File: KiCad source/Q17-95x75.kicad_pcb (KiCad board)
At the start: 2 copper layers, 96.5 x 76.2 mm, 84 parts, among them J1 TerminalBlock, Q1 IRF610, Q10 KSA992, Q11 BS250P, Q12 KSC1845, Q13 IRF610, Q14 IRF9610, Q15 FQA46N15, Q16 FQA36P15, Q2 KSA992, Q3 KSC1845, Q4 IRF9610, Q5 IRF9610, Q6 IRF610, Q7 KSC1845, Q8 2N7000, Q9 BS250P, U1 DIP-8_W7.62mm_Socket, U1 OPA1641

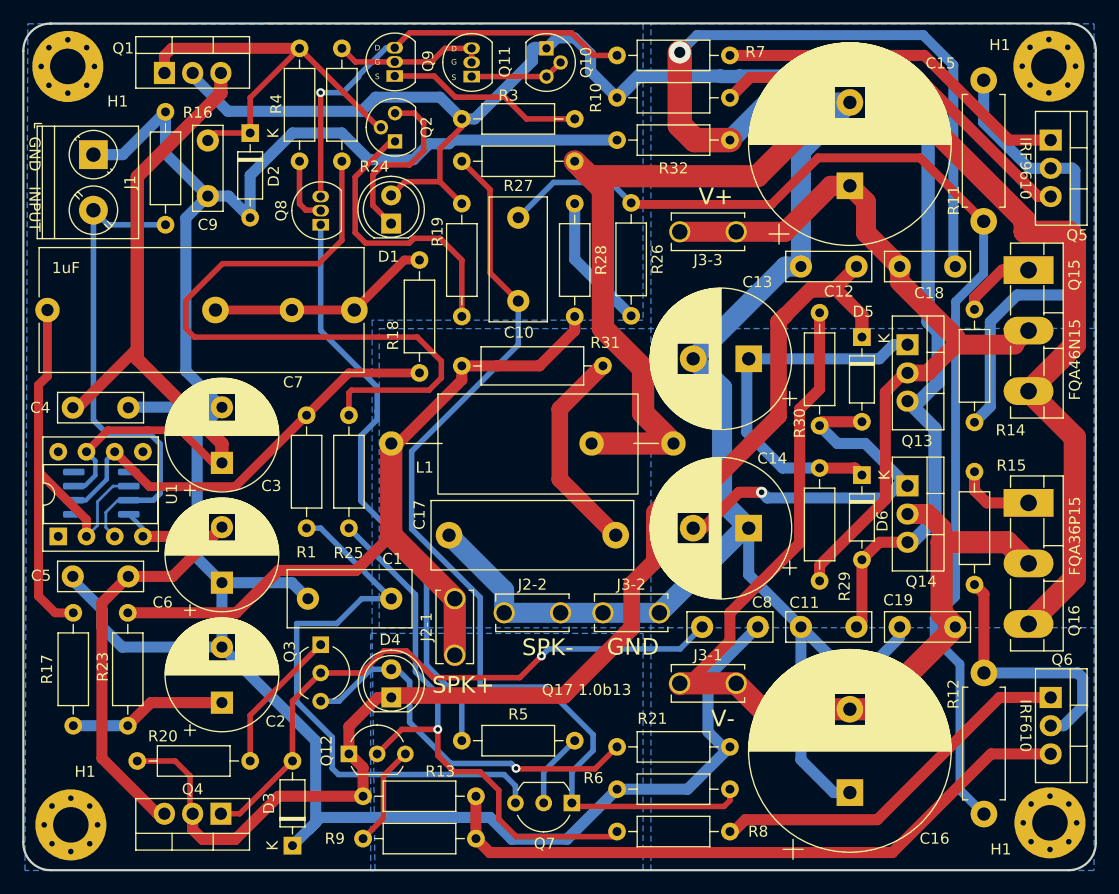
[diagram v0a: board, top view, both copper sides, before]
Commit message: Update PCB to 1.0b15
- Change Q12 footprint to TO-126.
- More cleanup of tracks.
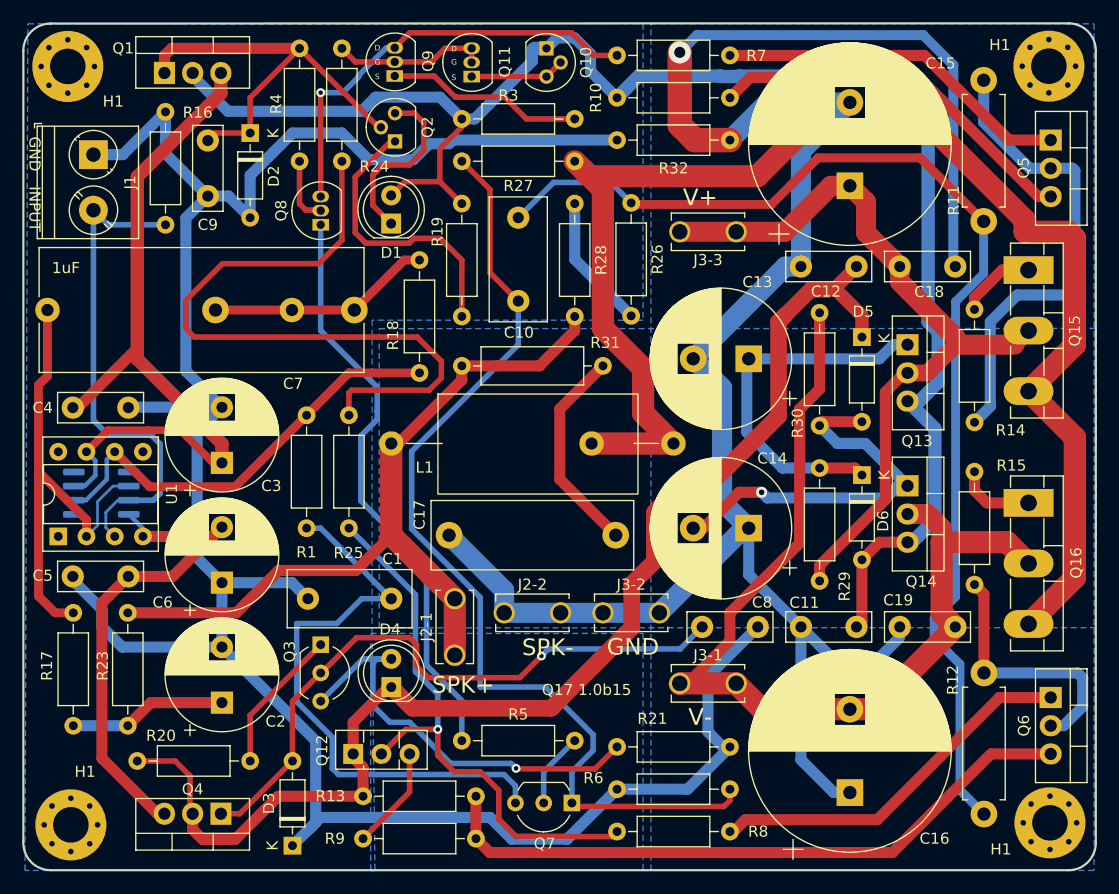
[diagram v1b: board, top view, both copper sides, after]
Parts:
- Q12: value KSC1845 -> BD139; footprint Package_TO_SOT_THT:TO-92_Inline_Wide -> Package_TO_SOT_THT:TO-126-3_Vertical
- moved D4 0.93 mm to (124.7, 111.8)
- moved Q12 0.38 mm to (121.3, 117.8)
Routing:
- net Net-(D4-Pad2): track 34.5 -> 38.7 mm
- net Net-(C8-Pad2): track 55.4 -> 57.5 mm
- net Net-(C12-Pad2): track 111.4 -> 112.3 mm
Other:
- board text added: "Q17 1.0b15"
- board text added: "QUAD405 Audiophile Tiberiu Vicol PCB Design by Stef PROTO RELEASE"
- board text removed: "FQA36P15"
- board text removed: "FQA46N15"
- board text removed: "IRF610"
- board text removed: "IRF9610"
- board text removed: "Q17 1.0b13"
- board text removed: "QUAD405 Audiophile Tiberiu Vicol PCB Design by Stef"

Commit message: PCB and diagram v1.0.b16
- Replaced Q12 by BD139 and TO-126 footprint.
- Optimisation of ground plane.
- Add of missing R2 (yes after 16 beta!!).
- Changed footprint of C7.
- Add some 3D pictures.
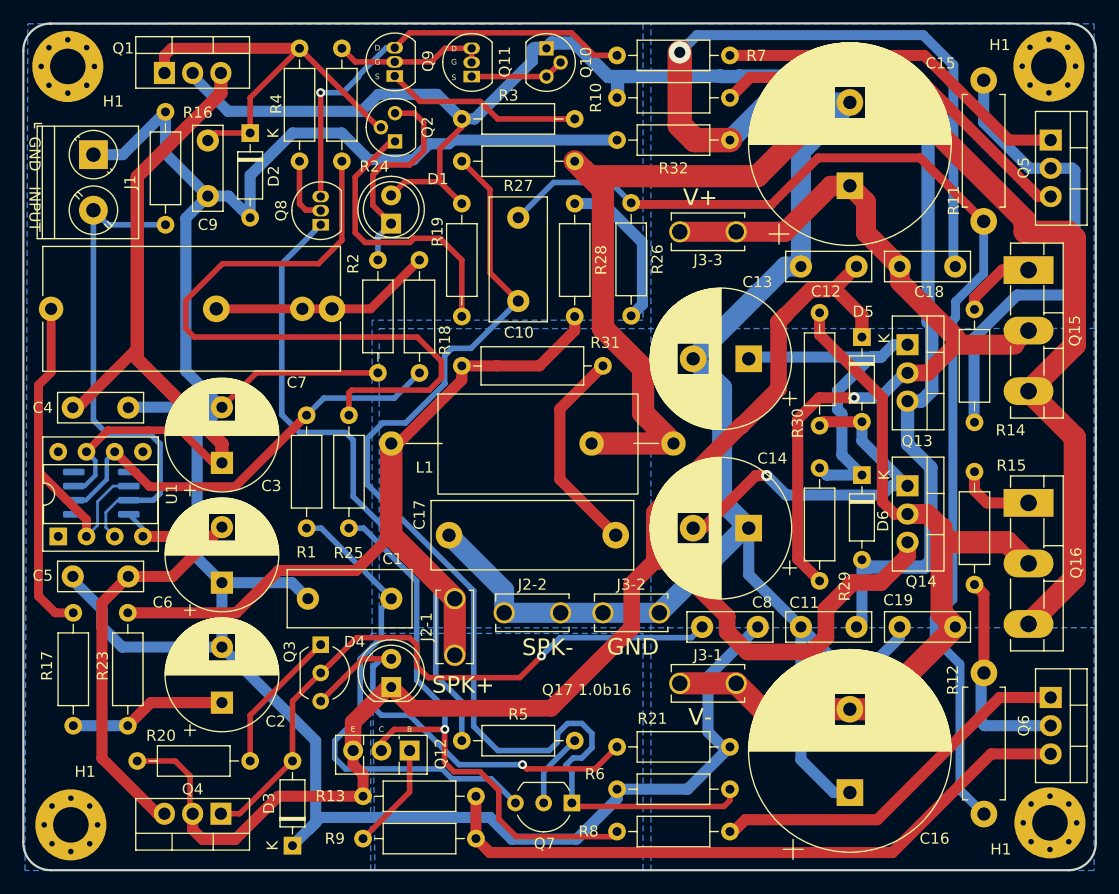
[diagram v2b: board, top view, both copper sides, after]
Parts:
- added R2: 5k6/1W, Resistor_THT:R_Axial_DIN0207_L6.3mm_D2.5mm_P10.16mm_Horizontal, F.Cu at (123.5, 73.3)
- J1: value TerminalBlock -> Input
- Q1, Q13, Q6: value IRF610 -> FQP3N30
- Q4, Q5: value IRF9610 -> FQP3P20
- U1: value DIP-8_W7.62mm_Socket -> OPA1641
- moved Q12 5.09 mm to (126.4, 117.5), turned to 180 degrees
- moved C7 3.52 mm to (94.0, 77.7)
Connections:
- Q12 pad 1: Net-(C12-Pad2) -> Net-(R9-Pad1)
- Q12 pad 3: Net-(Q12-Pad3) -> Net-(C12-Pad2)
- Q14 pad 3: Net-(C11-Pad2) -> Net-(C12-Pad2)
- R9 pad 1: Net-(Q12-Pad3) -> Net-(R9-Pad1)
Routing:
- net Net-(C12-Pad2): track 112.3 -> 144.4 mm
- net Net-(C16-Pad2): track 89.5 -> 72.4 mm
- net GND: track 222.3 -> 238.1 mm
- net Net-(C10-Pad2): track 90.4 -> 101.7 mm
- net Net-(R9-Pad1): track 0.00 -> 9.66 mm
- net Net-(Q12-Pad3): track 9.36 -> 0.00 mm
- net Net-(C1-Pad1): track 52.7 -> 44.7 mm
- net Net-(C15-Pad1): track 70.6 -> 75.4 mm, vias 0 -> 1
- net Net-(Q6-Pad2): track 23.5 -> 19.2 mm
- net Net-(Q8-Pad1): track 53.0 -> 57.0 mm
- net Net-(D1-Pad1): track 16.0 -> 19.8 mm
- net Net-(C14-Pad2): track 36.1 -> 33.7 mm
- net Net-(R26-Pad2): track 12.2 -> 14.6 mm
- net Net-(R25-Pad2): track 50.6 -> 52.4 mm
- net Net-(C11-Pad2): track 146.7 -> 147.9 mm
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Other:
- board text added: "B"
- board text added: "C"
- board text added: "E"
- board text added: "Q17 1.0b16"
- board text removed: "1uF"
- board text removed: "Q17 1.0b15"

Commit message: PCB 1.0b17
Moved Q12 to the border of the board.
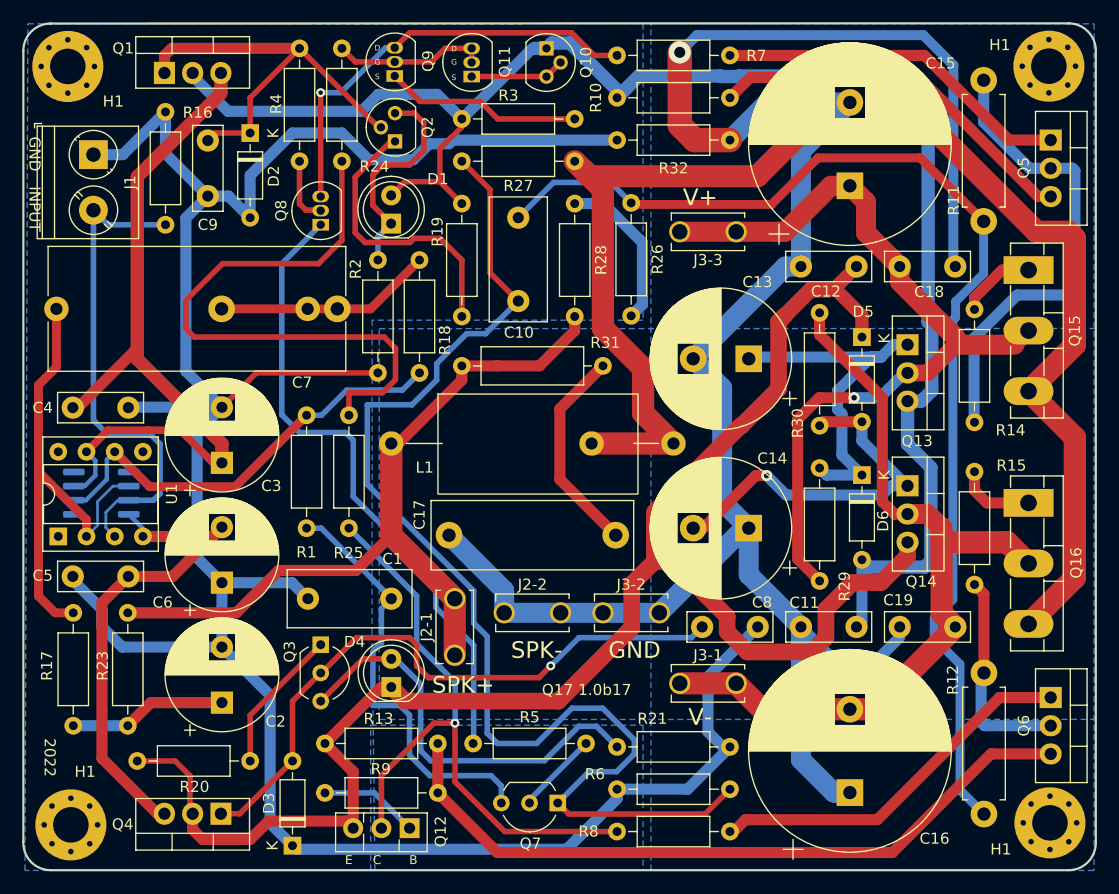
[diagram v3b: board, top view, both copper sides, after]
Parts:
- moved Q12 6.98 mm to (126.4, 124.5)
- moved R13 5.86 mm to (128.9, 116.8)
- moved R9 5.36 mm to (118.7, 121.3)
- moved Q7 1.27 mm to (139.7, 122.2)
- moved R5 1.05 mm to (132.1, 116.8)
- moved C7 0.48 mm to (94.5, 77.7)
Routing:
- net Net-(C10-Pad2): track 101.7 -> 110.0 mm
- net Net-(R24-Pad2): track 62.5 -> 55.1 mm
- net Net-(C1-Pad1): track 44.7 -> 38.7 mm
- net Net-(Q6-Pad3): track 59.7 -> 65.5 mm
- net Net-(R25-Pad2): track 52.4 -> 56.5 mm
- net GND: track 238.1 -> 235.1 mm
- net Net-(C12-Pad2): track 144.4 -> 147.3 mm
- net Net-(D4-Pad2): track 38.6 -> 37.6 mm, vias 1 -> 0
- net Net-(R9-Pad1): track 9.66 -> 8.94 mm
- net Net-(Q8-Pad1): track 57.0 -> 57.7 mm
- net Net-(Q7-Pad2): track 6.77 -> 7.46 mm
- net Net-(L1-Pad2): track 128.0 -> 127.4 mm
- net Net-(C11-Pad2): track 147.9 -> 147.4 mm
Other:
- board text added: "2022"
- board text added: "Q17 1.0b17"
- board text removed: "Q17 1.0b16"
